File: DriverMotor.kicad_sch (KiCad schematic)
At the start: 44 parts, among them U10 DRV8874PWPR, U15 WE-TVS-82400102, U16 SN74LVC2G14DBV, U17 WE-TVS-82400102, U18 SN74LVC2G14DBV

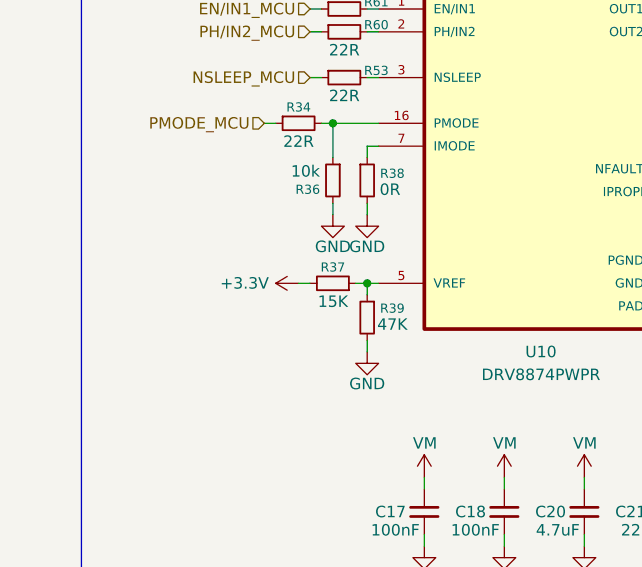
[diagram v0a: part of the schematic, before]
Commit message: feat : add SMLVN6RGB status LED stage with balanced 3.3V ballast resistors
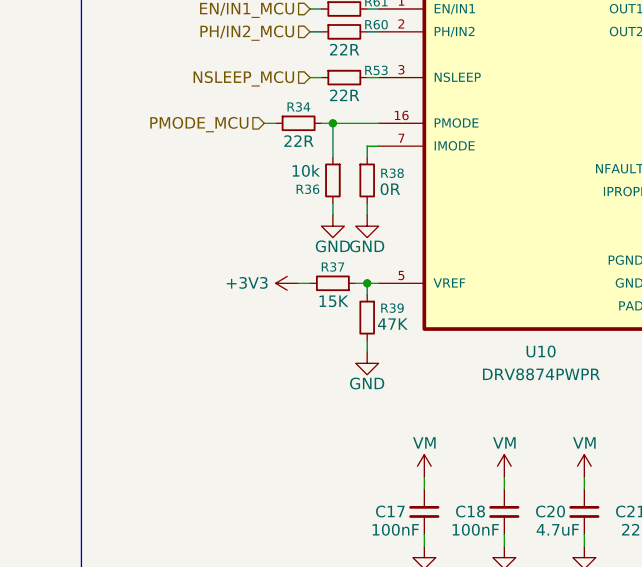
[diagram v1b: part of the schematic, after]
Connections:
- net +3.3V: no longer R37.2
- net +3V3: now also R37.2
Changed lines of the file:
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@@
 			)
 		)
-		(property "Value" "+3.3V"
+		(property "Value" "+3V3"
 			(at 42.418 82.55 90)
 			(show_name no)

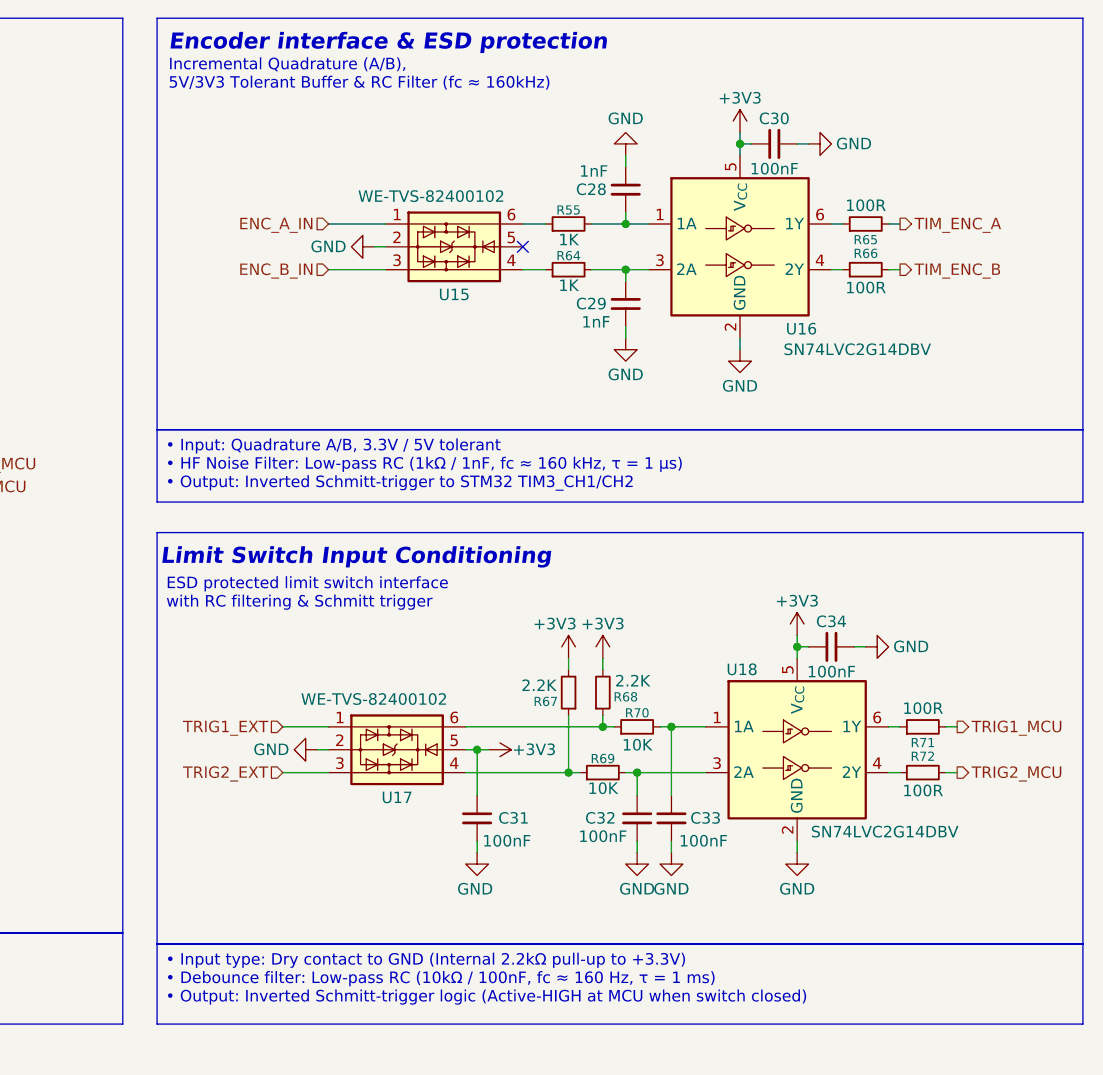
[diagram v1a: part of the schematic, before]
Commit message: feat: switch to JST-GH connectors and add TPD4E05U06 TVS protection for SPI/I2C
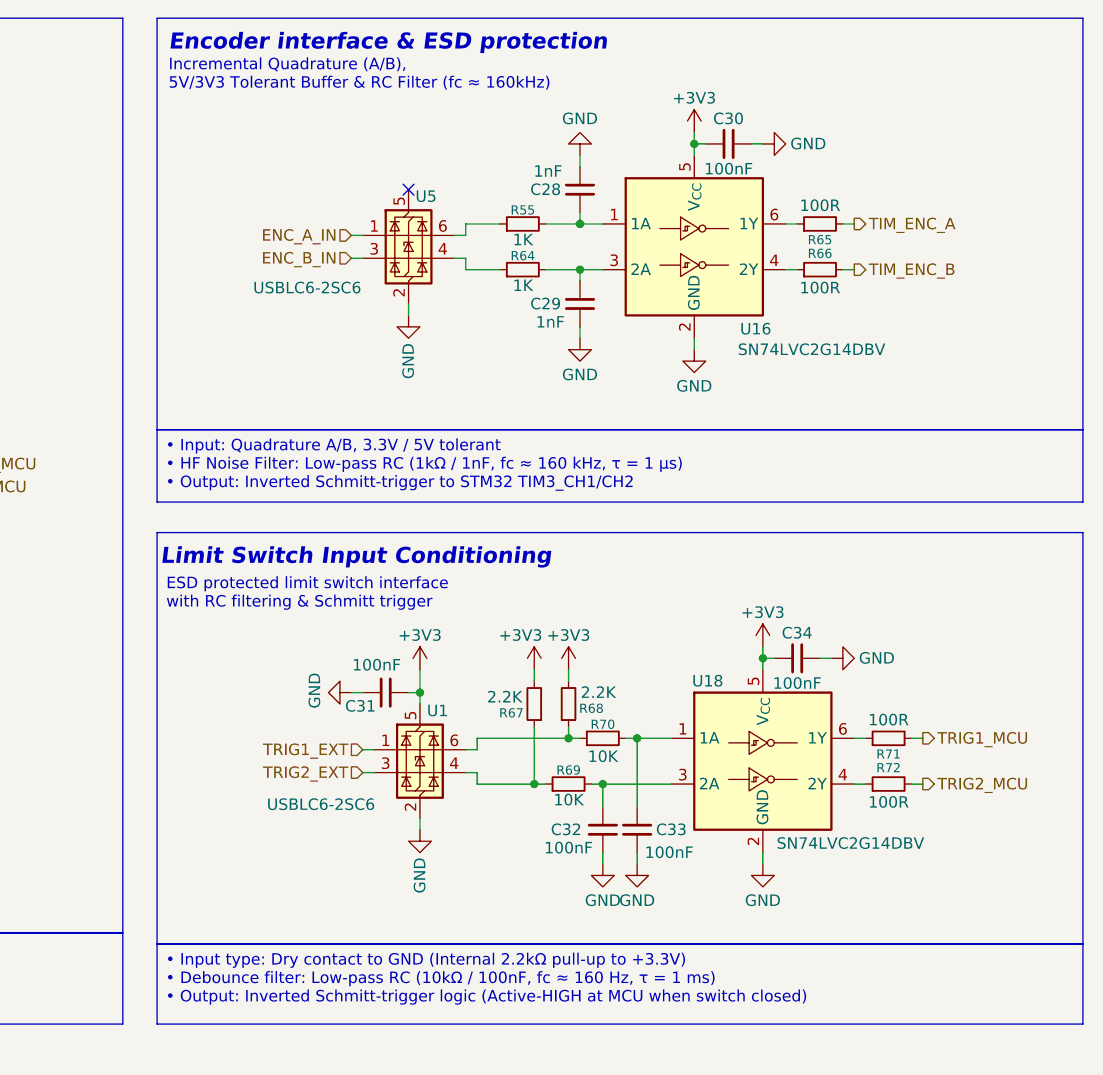
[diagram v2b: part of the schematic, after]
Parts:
- removed U15, U17: WE-TVS-82400102, Package_TO_SOT_SMD:SOT-23-6, symbol Power_Protection:WE-TVS-82400102
- added U1, U5: USBLC6-2SC6, Package_TO_SOT_SMD:SOT-23-6, symbol Power_Protection:USBLC6-2SC6
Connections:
- net +3V3: now also U1.5 (VBUS)
- net ENC_A_IN: now also U5.1 (I/O1)
- net ENC_B_IN: now also U5.3 (I/O2)
- net GND: now also U1.2 (GND), U5.2 (GND)
- net TRIG1_EXT: now also U1.1 (I/O1)
- net TRIG2_EXT: now also U1.3 (I/O2)
- net at R67.1, R69.1: now also U1.4 (I/O2)
- net at R68.1, R70.1: now also U1.6 (I/O1)
- net at R64.1: now also U5.4 (I/O2)
- net at R55.1: now also U5.6 (I/O1)
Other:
- moved on the sheet: C28, C29, C30, C31, C32, C33, C34, R55, R64, R65, R66, R67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

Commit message: feat: add SPI connector and I²c pull up for magnetic encoder
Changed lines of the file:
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@@
 		)
 		(property "Value" "100nF"
-			(at 185.166 113.03 0)
+			(at 185.166 112.522 0)
 			(show_name no)
 			(do_not_autoplace no)
@@
 		)
 		(property "Value" "GND"
-			(at 156.21 58.42 90)
+			(at 156.21 57.15 0)
 			(show_name no)
 			(do_not_autoplace no)
@@
 		)
 		(property "Value" "GND"
-			(at 157.48 115.57 90)
+			(at 157.48 114.3 0)
 			(show_name no)
 			(do_not_autoplace no)
@@
 		(dnp no)
 		(property "Reference" "R72"
-			(at 209.55 103.632 90)
+			(at 209.55 103.886 90)
 			(show_name no)
 			(do_not_autoplace no)

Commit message: feat: finalize STM32G070CBT6 LQFP48 pinout and peripheral mapping
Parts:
- R65, R66, R71, R72: value 100R -> 22R
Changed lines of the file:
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@@
 			)
 		)
-		(property "Value" "100R"
+		(property "Value" "22R"
 			(at 209.55 98.298 90)
 			(show_name no)
@@
 			)
 		)
-		(property "Value" "100R"
+		(property "Value" "22R"
 			(at 201.93 50.292 90)
 			(show_name no)
@@
 			)
 		)
-		(property "Value" "100R"
+		(property "Value" "22R"
 			(at 209.55 107.442 90)
 			(show_name no)
@@
 			)
 		)
-		(property "Value" "100R"
+		(property "Value" "22R"
 			(at 201.93 41.148 90)
 			(show_name no)
